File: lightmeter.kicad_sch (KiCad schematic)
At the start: 12 parts, among them J1 USB_C_Receptacle_USB2.0_16P, J2 5V input, U2 ESP32-S3-WROOM-1

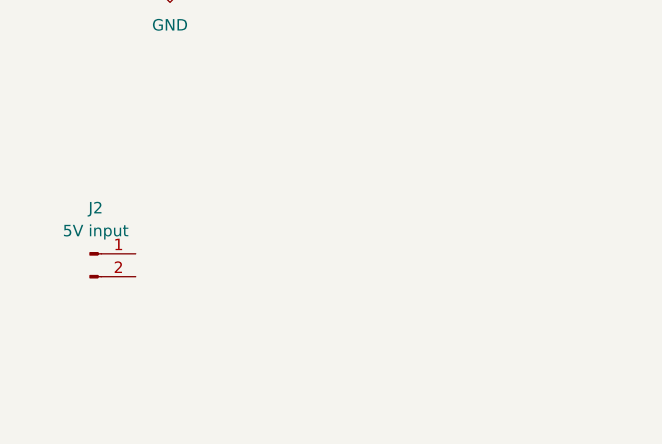
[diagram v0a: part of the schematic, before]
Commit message: Added power supply block to the schematic
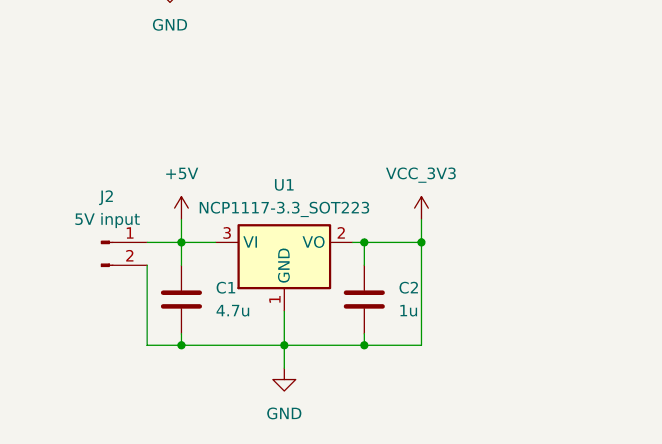
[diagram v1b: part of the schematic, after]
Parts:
- added C1: 4.7u, symbol Device:C
- added C2: 1u, symbol Device:C
- added U1: NCP1117-3.3_SOT223, Package_TO_SOT_SMD:SOT-223-3_TabPin2, symbol Regulator_Linear:NCP1117-3.3_SOT223
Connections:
- net VCC_3V3 is gone; now on net GND: C3.1, C4.1, R24.1
- net +5V: now also J2.1 (Pin_1), C1.1, U1.3 (VI)
- net GND: now also J2.2 (Pin_2), C1.2, C2.1, C2.2, U1.1 (GND), U1.2 (VO)
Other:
- moved on the sheet: J2

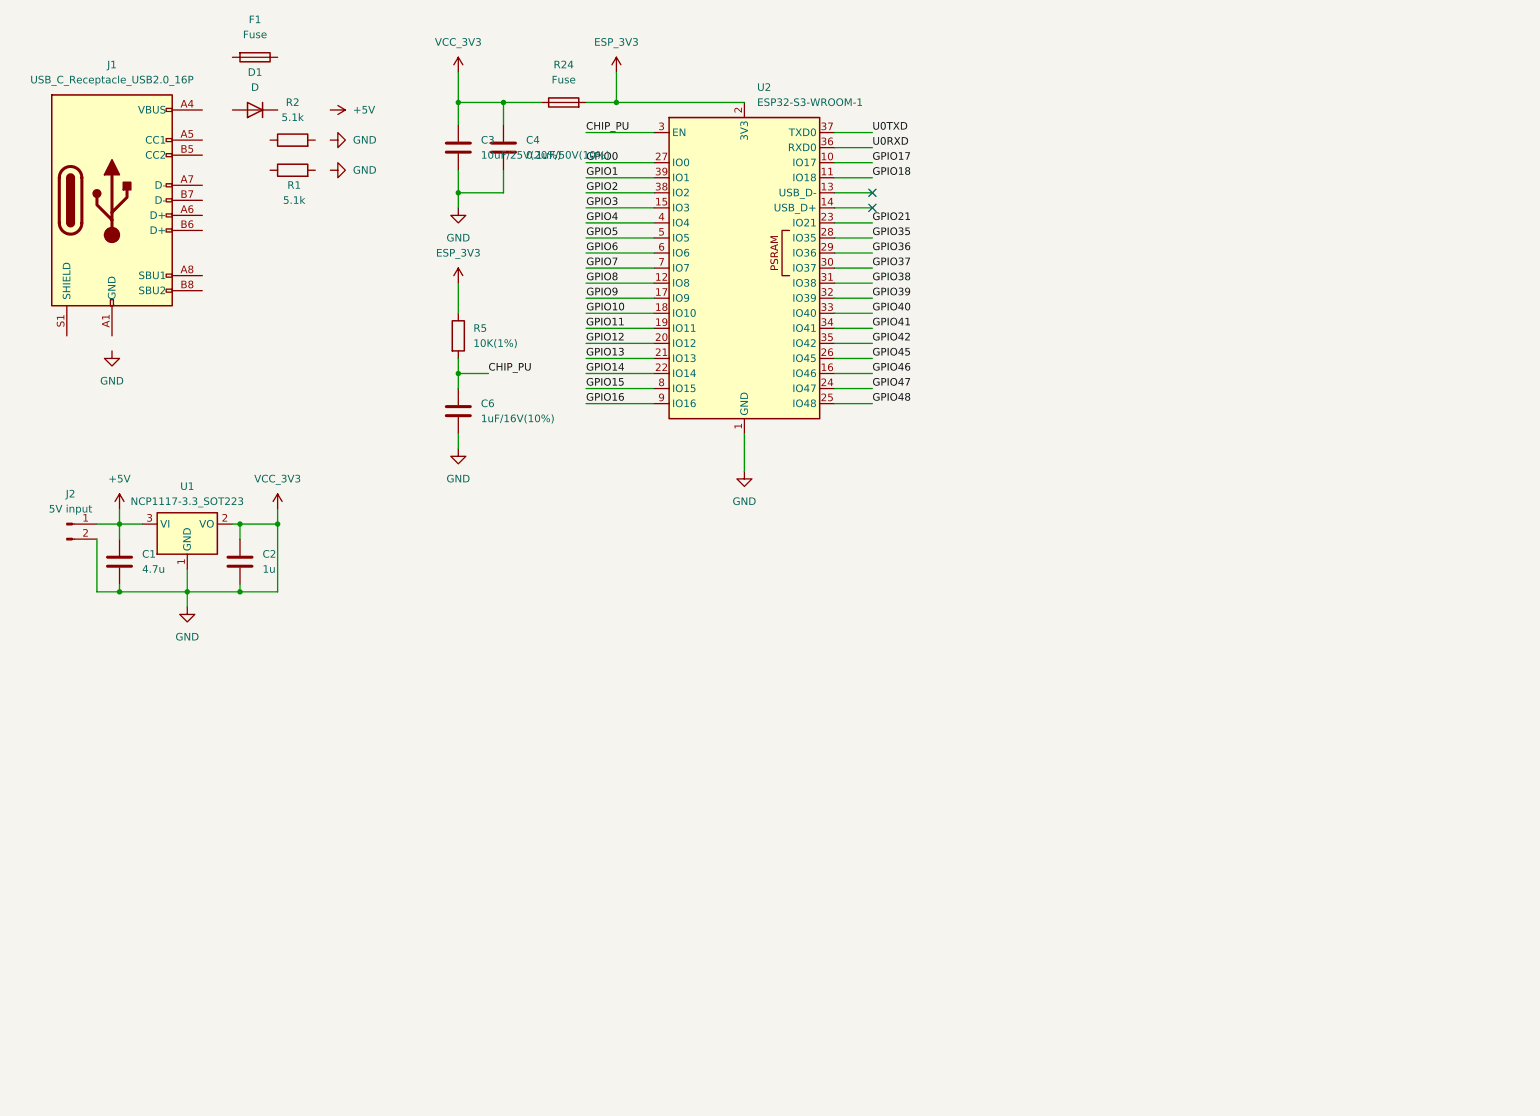
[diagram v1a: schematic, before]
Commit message: Added the Rotary encoders and the push buttons, that are going to be used, in the schematic.
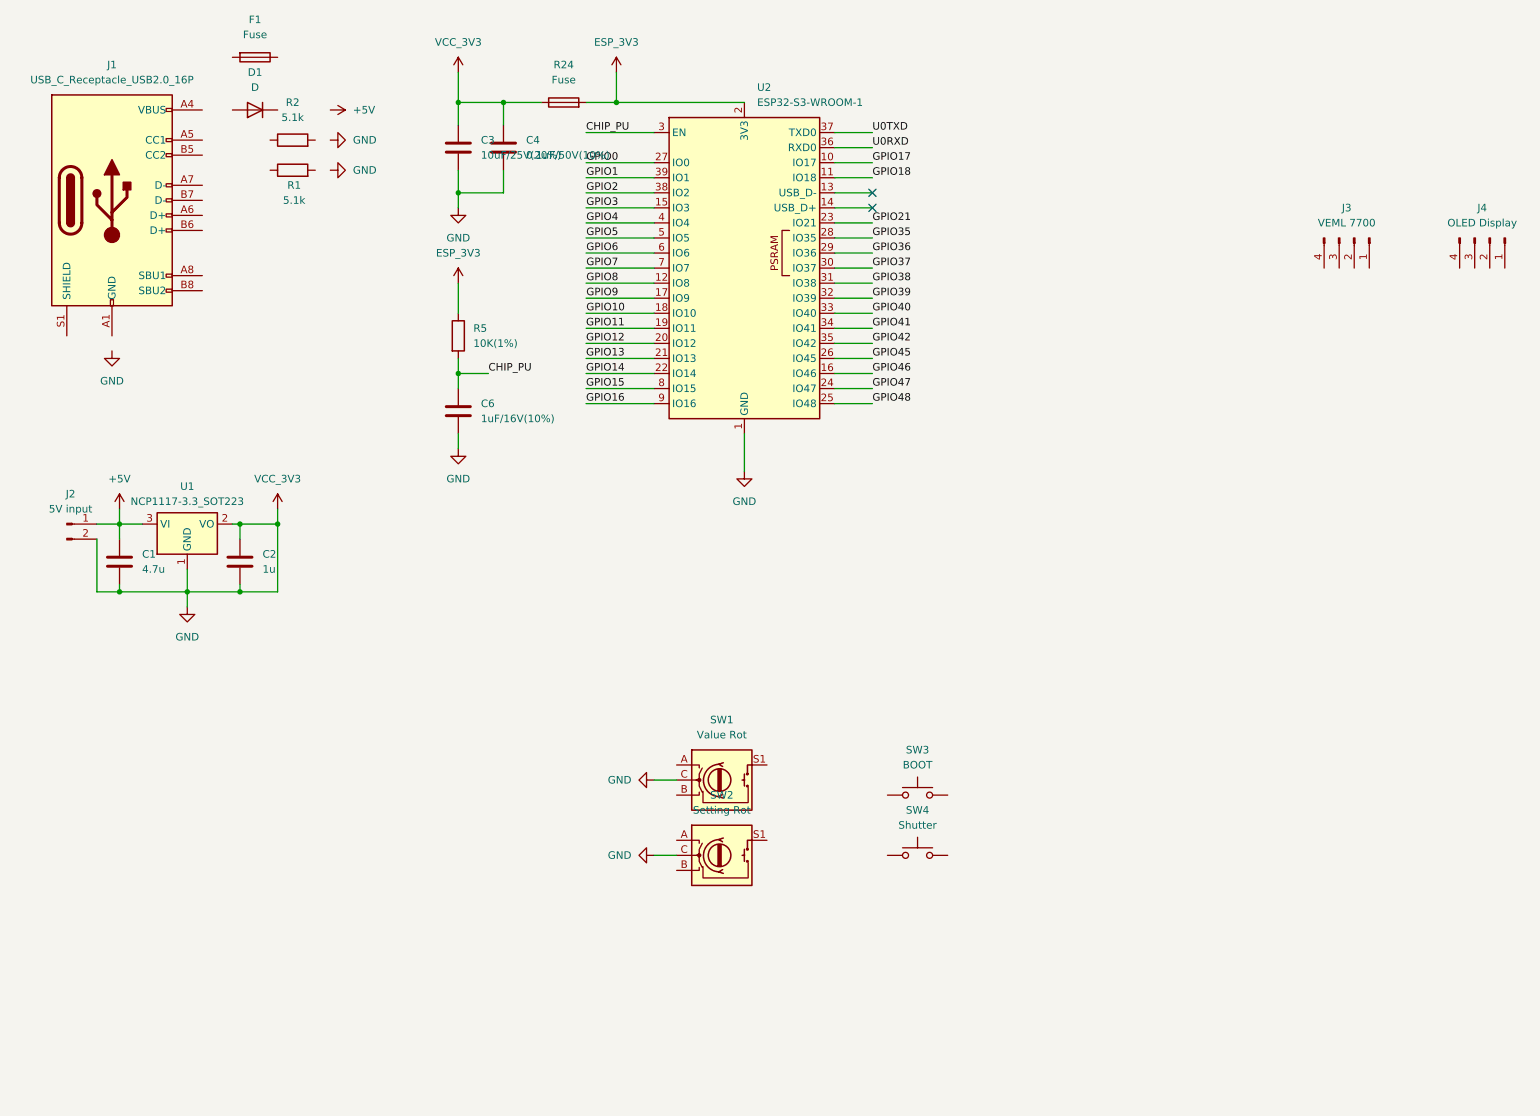
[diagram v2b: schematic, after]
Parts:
- added J3: VEML 7700, symbol Connector:Conn_01x04_Pin
- added J4: OLED Display, symbol Connector:Conn_01x04_Pin
- added SW1: Value Rot, symbol Device:RotaryEncoder_Switch
- added SW2: Setting Rot, symbol Device:RotaryEncoder_Switch
- added SW3: BOOT, symbol Switch:SW_Push
- added SW4: Shutter, symbol Switch:SW_Push
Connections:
- net GND: now also SW1.C, SW2.C

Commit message: Finished schematic. Layout is next
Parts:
- removed J3: VEML 7700, symbol Connector:Conn_01x04_Pin
- removed J4: OLED Display, symbol Connector:Conn_01x04_Pin
- added C10, C5, C7, C8, C9: 0.1u, symbol Device:C
- added J3: VEML7700, symbol Connector:Conn_01x05_Socket
- added J4: Conn_01x04_Socket, symbol Connector:Conn_01x04_Socket
- added J5: BoostConverterInput, symbol Connector:Conn_01x02_Pin
- added R12, R13, R14, R15, R16, R17, R3, R4, R6, R7, R8: 10k, symbol Device:R
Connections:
- net +5V: now also D1.1 (K), F1.1, J5.1 (Pin_1)
- net ESP_3V3: now also J3.5 (Pin_5), J4.2 (Pin_2), R12.1, R15.2, R16.1, R17.1, R4.1, R6.2, R8.2
- net GND: now also J1.A1 (GND), J1.A12 (GND), J1.B1 (GND), J1.B12 (GND), R1.2, R2.2, SW3.1, SW4.1, C10.1, C5.1, C7.1, C8.1, C9.1, J3.3 (Pin_3), J4.1 (Pin_1), J5.2 (Pin_2)
- net GPIO0: now also SW3.2, C10.2
- net GPIO10: now also C5.2, R7.1
- net GPIO11: now also C8.2, R13.1
- net GPIO13: now also SW1.S1, R12.2
- net GPIO14: now also SW2.S1, R17.2
- net GPIO21: now also C7.2, R3.1
- net GPIO36: now also C9.2, R14.1
- net GPIO4: now also SW4.2, R8.1
- net GPIO8: now also J3.1 (Pin_1), J4.4 (Pin_4)
- net GPIO9: now also J3.2 (Pin_2), J4.3 (Pin_3)
- net GPIO19: now reaches U2.13 (USB_D-)
- net GPIO19: now also J1.A7 (D-), J1.B7 (D-)
- net GPIO20: now reaches U2.14 (USB_D+)
- net GPIO20: now also J1.A6 (D+), J1.B6 (D+)
- net at F1.2: now also D1.2 (A), J1.A4 (VBUS), J1.A9 (VBUS), J1.B4 (VBUS), J1.B9 (VBUS)
- net at SW1.A: now also R6.1, R7.2
- net at SW1.B: now also R3.2, R4.2
- net at J1.A5 (CC1): now also R2.1
- net at J1.B5 (CC2): now also R1.1
- net at SW2.A: now also R13.2, R15.1
- net at SW2.B: now also R14.2, R16.2
- no-connect marks 2 -> 3
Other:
- moved on the sheet: C1, C2, C3, C4, C6, J2, R1, R2, R24, R5, SW1, SW2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

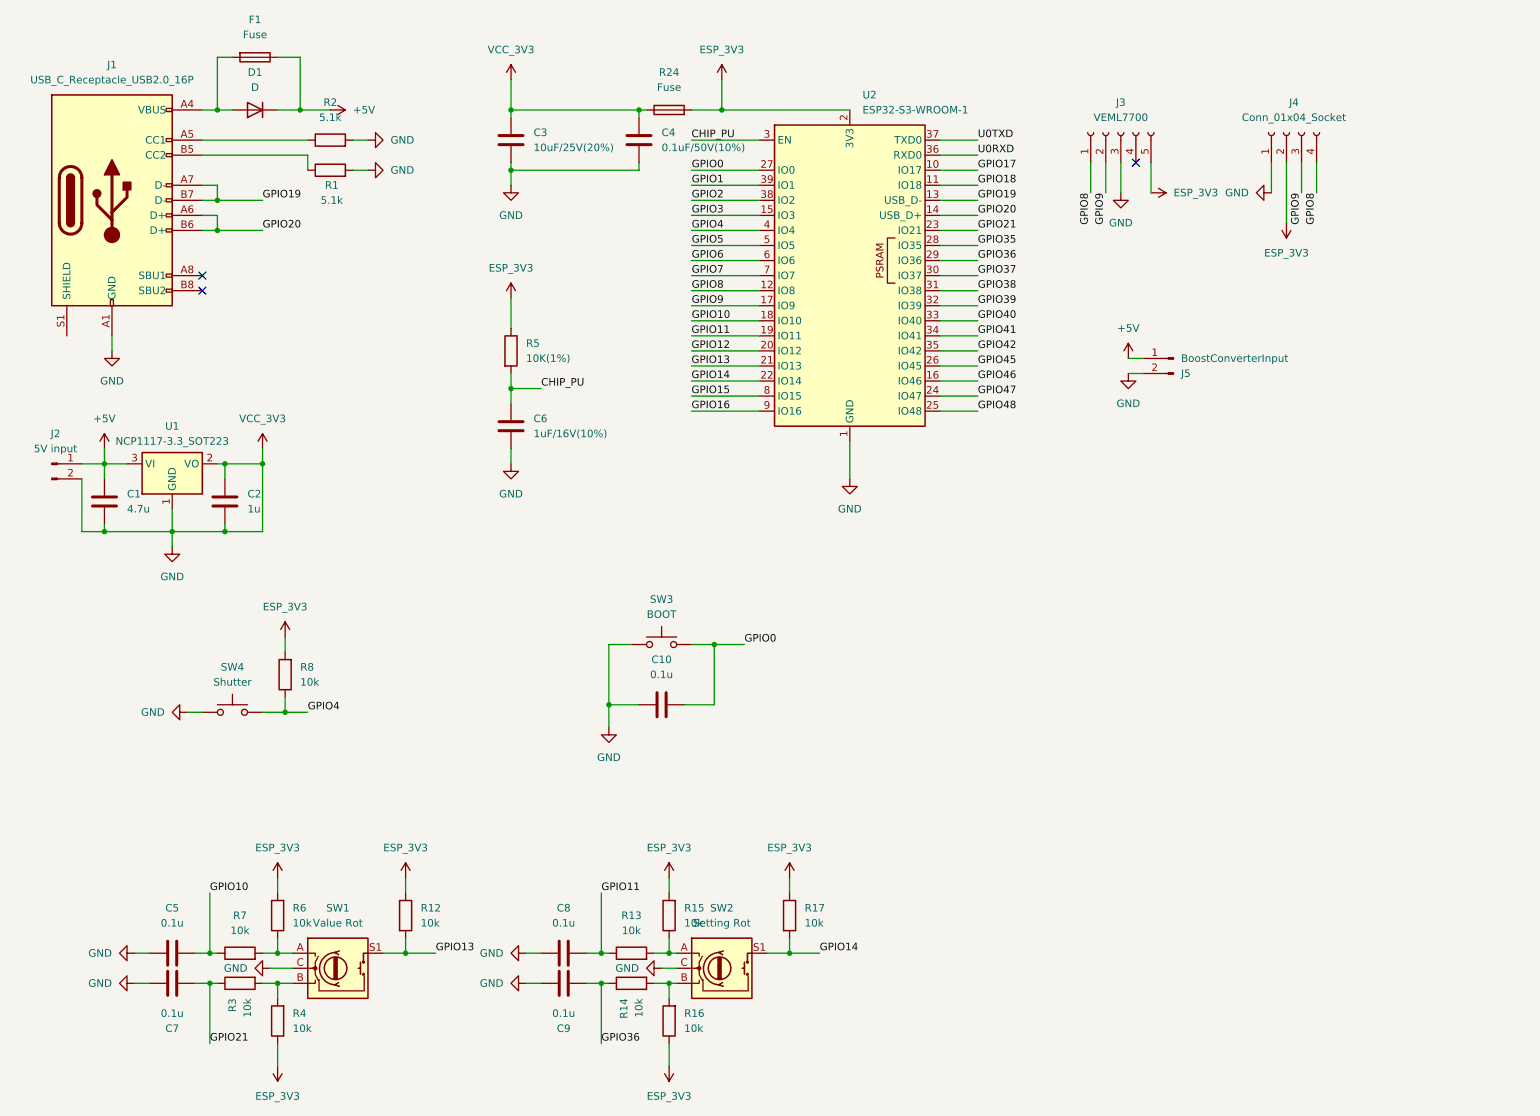
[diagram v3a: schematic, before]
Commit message: Replaced the usb C port with a connector for a programmer module
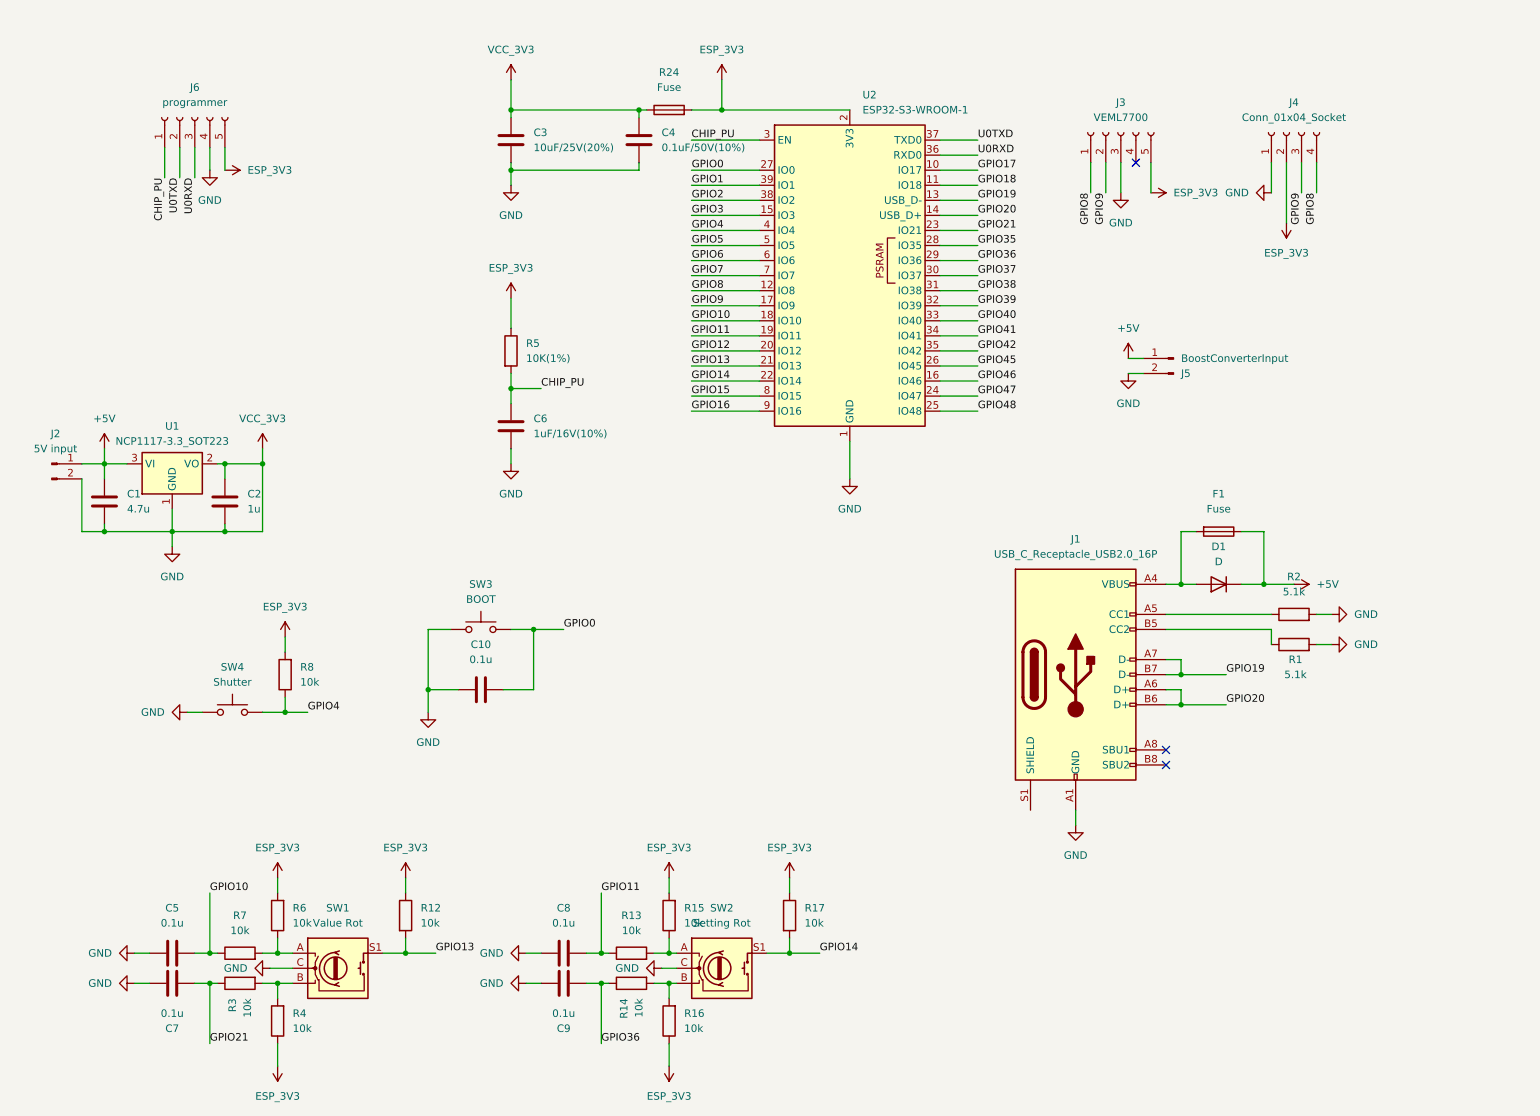
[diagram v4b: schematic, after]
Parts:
- added J6: programmer, symbol Connector:Conn_01x05_Socket
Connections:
- net CHIP_PU: now also J6.1 (Pin_1)
- net ESP_3V3: now also J6.5 (Pin_5)
- net GND: now also J6.4 (Pin_4)
- net U0RXD: now also J6.3 (Pin_3)
- net U0TXD: now also J6.2 (Pin_2)
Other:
- moved on the sheet: C10, D1, F1, J1, R1, R2, SW3

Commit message: Annotated the schematic
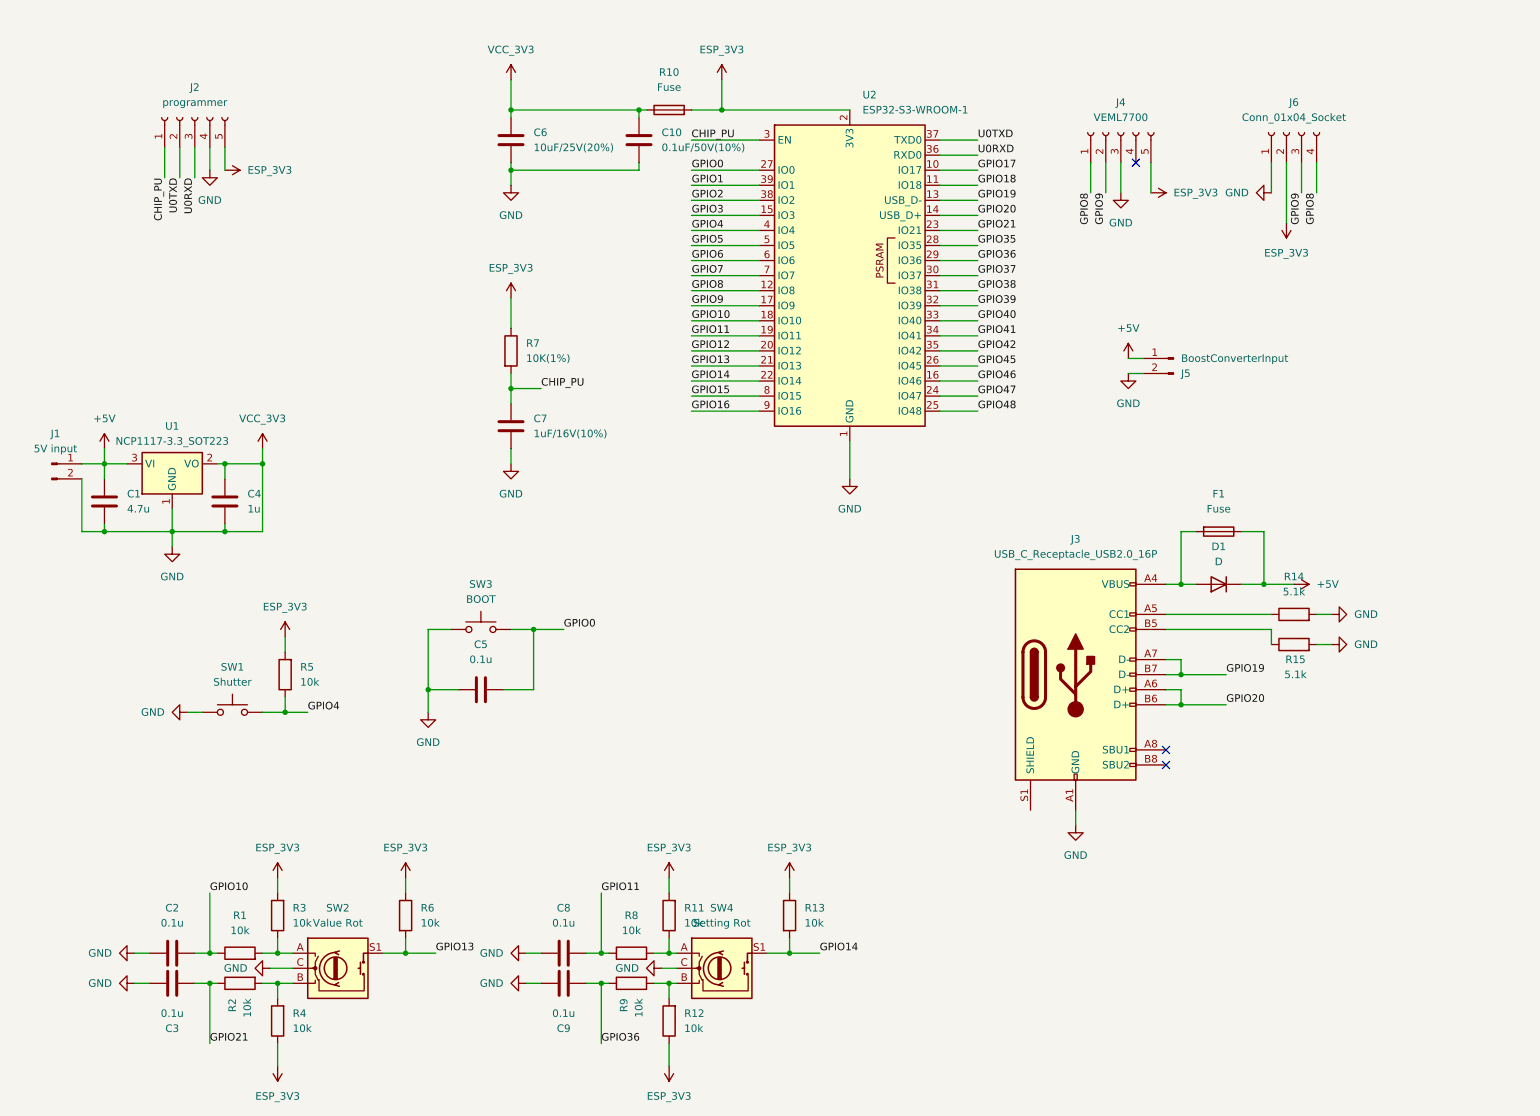
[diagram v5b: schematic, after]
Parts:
- renumbered C4 to C10, C5 to C2, C7 to C3, C2 to C4, C10 to C5, C3 to C6, C6 to C7, J2 to J1, J6 to J2, J1 to J3, J3 to J4, J4 to J6, R7 to R1, R24 to R10, R15 to R11, R16 to R12, R17 to R13, R2 to R14, R1 to R15, R3 to R2, R6 to R3, R8 to R5, R12 to R6, R5 to R7, R13 to R8, R14 to R9, SW4 to SW1, SW1 to SW2, SW2 to SW4
